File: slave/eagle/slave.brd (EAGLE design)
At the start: 55.5 x 30.5 mm, 17 parts, among them IC1 AT90S2313S, IC2 5V, Q1 3,686411M

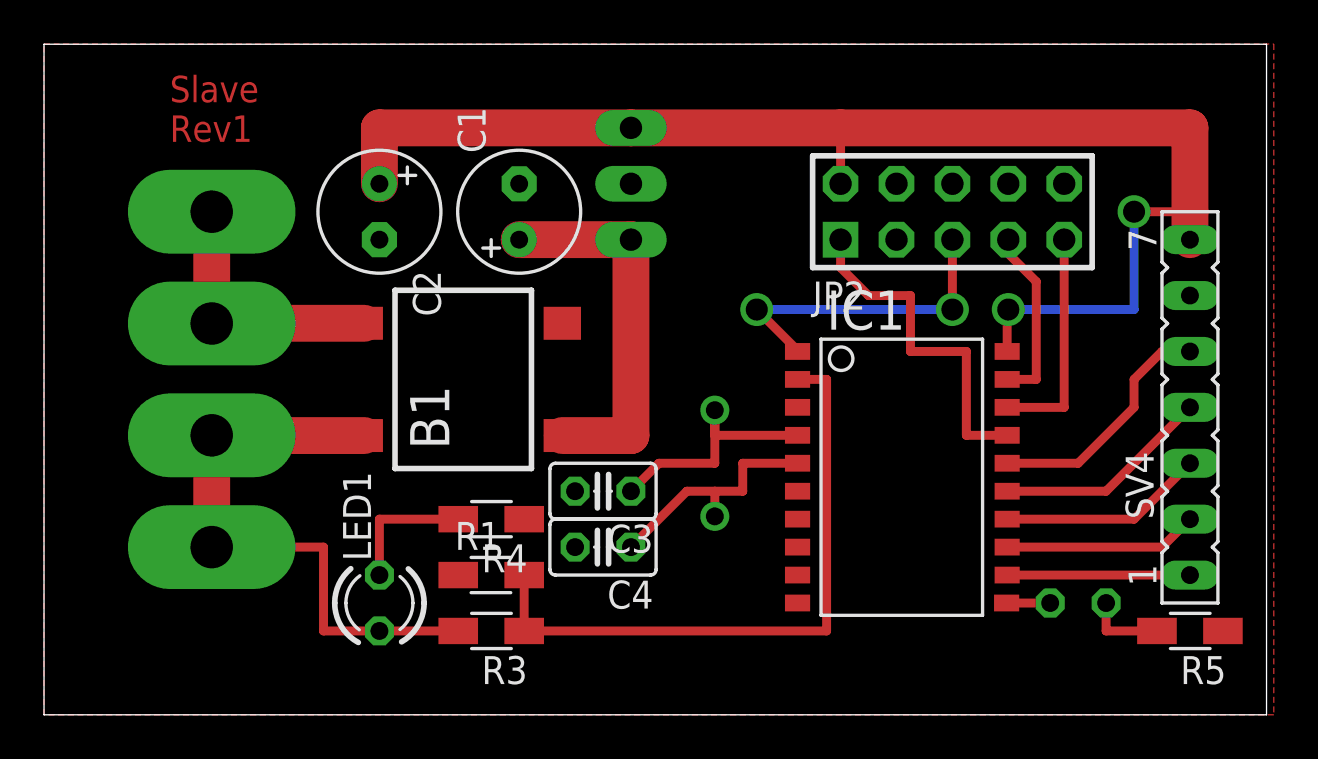
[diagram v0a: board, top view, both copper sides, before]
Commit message: New directory structure + add slave state machine without any further logic
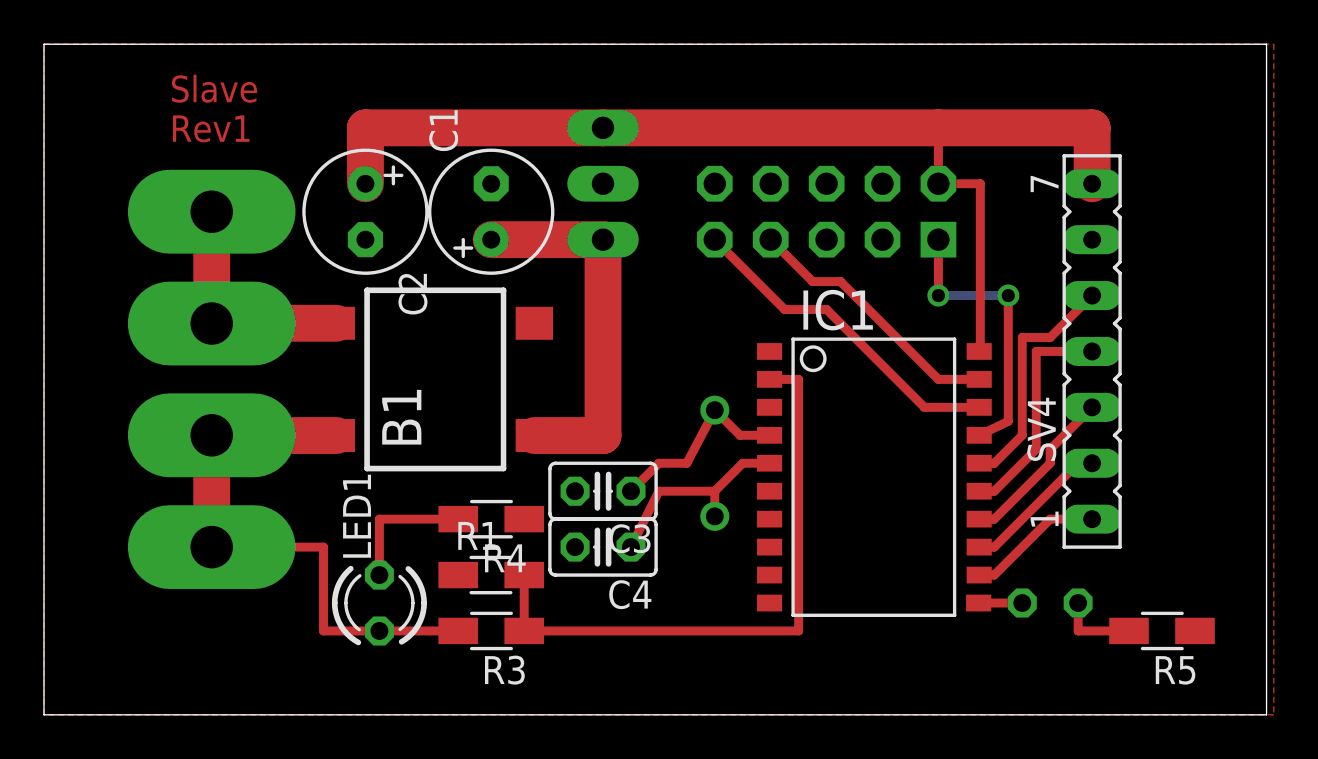
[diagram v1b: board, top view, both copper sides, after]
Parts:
- moved JP2 5.71 mm to (33.0, 20.3), flipped to the bottom
- moved SV4 5.12 mm to (45.1, 14.0)
- moved IC2 1.27 mm to (25.4, 21.6)
- moved LED2 1.27 mm to (43.2, 2.54)
- moved R5 1.27 mm to (48.3, 1.27)
- moved B1 1.27 mm to (15.2, 12.7)
- moved C1 1.27 mm to (17.8, 20.3)
- moved IC1 1.27 mm to (35.6, 8.89)
- moved C2 0.63 mm to (12.1, 20.3)
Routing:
- net N$15: track 14.7 -> 0.00 mm, vias 2 -> 0
- net VCC: track 61.6 -> 50.2 mm, vias 2 -> 0
- net N$13: track 10.2 -> 15.2 mm
- net N$12: track 8.20 -> 12.1 mm
- net N$7: track 11.7 -> 8.76 mm
- net N$14: track 15.7 -> 12.9 mm, vias 0 -> 2
- net N$8: track 8.83 -> 6.71 mm
- net N$5: track 8.31 -> 6.18 mm
- net N$9: track 9.36 -> 7.61 mm
- net N$16: track 11.0 -> 9.54 mm
- net N$2: track 29.0 -> 27.8 mm
- net N$10: track 12.0 -> 10.8 mm
- net N$6: track 27.0 -> 25.8 mm
